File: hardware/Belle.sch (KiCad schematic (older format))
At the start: 18 parts, among them P1 Bell CONN, P2 Battery CONN, P3 Flashing CONN, U1 74AHC1G14, U2 ESP-12, U3 AP2112

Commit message: fix
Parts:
- C3, C4: footprint (none) -> Capacitors_SMD:C_1206_HandSoldering
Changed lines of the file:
@@
 $EndComp
 $Comp
-L GND #PWR8
+L GND #PWR01
 U 1 1 58BBCCFC
 P 5900 4700
-F 0 "#PWR8" H 5900 4450 50  0001 C CNN
+F 0 "#PWR01" H 5900 4450 50  0001 C CNN
 F 1 "GND" H 5900 4550 50  0000 C CNN
 F 2 "" H 5900 4700 50  0000 C CNN
@@
 $EndComp
 $Comp
-L +3.3V #PWR7
+L +3.3V #PWR02
 U 1 1 58BBCD12
 P 5900 2800
-F 0 "#PWR7" H 5900 2650 50  0001 C CNN
+F 0 "#PWR02" H 5900 2650 50  0001 C CNN
 F 1 "+3.3V" H 5900 2940 50  0000 C CNN
 F 2 "" H 5900 2800 50  0000 C CNN
@@
 $EndComp
 $Comp
-L GND #PWR9
+L GND #PWR03
 U 1 1 58BBCDC5
 P 6650 3000
-F 0 "#PWR9" H 6650 2750 50  0001 C CNN
+F 0 "#PWR03" H 6650 2750 50  0001 C CNN
 F 1 "GND" H 6650 2850 50  0000 C CNN
 F 2 "" H 6650 3000 50  0000 C CNN
@@
 $EndComp
 $Comp
-L GND #PWR5
+L GND #PWR04
 U 1 1 58BBD0DA
 P 3600 3800
-F 0 "#PWR5" H 3600 3550 50  0001 C CNN
+F 0 "#PWR04" H 3600 3550 50  0001 C CNN
 F 1 "GND" H 3600 3650 50  0000 C CNN
 F 2 "" H 3600 3800 50  0000 C CNN
@@
 $EndComp
 $Comp
-L +3.3V #PWR4
+L +3.3V #PWR05
 U 1 1 58BBD0F6
 P 3600 3150
-F 0 "#PWR4" H 3600 3000 50  0001 C CNN
+F 0 "#PWR05" H 3600 3000 50  0001 C CNN
 F 1 "+3.3V" H 3600 3290 50  0000 C CNN
 F 2 "" H 3600 3150 50  0000 C CNN
@@
 $EndComp
 $Comp
-L GND #PWR3
+L GND #PWR06
 U 1 1 58BBD1A3
 P 3100 4000
-F 0 "#PWR3" H 3100 3750 50  0001 C CNN
+F 0 "#PWR06" H 3100 3750 50  0001 C CNN
 F 1 "GND" H 3100 3850 50  0000 C CNN
 F 2 "" H 3100 4000 50  0000 C CNN
@@
 $EndComp
 $Comp
-L +3.3V #PWR1
+L +3.3V #PWR07
 U 1 1 58BBD349
 P 2400 2900
-F 0 "#PWR1" H 2400 2750 50  0001 C CNN
+F 0 "#PWR07" H 2400 2750 50  0001 C CNN
 F 1 "+3.3V" H 2400 3040 50  0000 C CNN
 F 2 "" H 2400 2900 50  0000 C CNN
@@
 $EndComp
 $Comp
-L GND #PWR2
+L GND #PWR08
 U 1 1 58BBD44E
 P 2400 3750
-F 0 "#PWR2" H 2400 3500 50  0001 C CNN
+F 0 "#PWR08" H 2400 3500 50  0001 C CNN
 F 1 "GND" H 2400 3600 50  0000 C CNN
 F 2 "" H 2400 3750 50  0000 C CNN
@@
 $EndComp
 $Comp
-L +3.3V #PWR6
+L +3.3V #PWR09
 U 1 1 58BBD4B2
 P 4350 3700
-F 0 "#PWR6" H 4350 3550 50  0001 C CNN
+F 0 "#PWR09" H 4350 3550 50  0001 C CNN
 F 1 "+3.3V" H 4350 3840 50  0000 C CNN
 F 2 "" H 4350 3700 50  0000 C CNN
@@
 $EndComp
 $Comp
-L +3.3V #PWR14
+L +3.3V #PWR010
 U 1 1 58BBD5B6
 P 7450 3900
-F 0 "#PWR14" H 7450 3750 50  0001 C CNN
+F 0 "#PWR010" H 7450 3750 50  0001 C CNN
 F 1 "+3.3V" H 7450 4040 50  0000 C CNN
 F 2 "" H 7450 3900 50  0000 C CNN
@@
 $EndComp
 $Comp
-L GND #PWR10
+L GND #PWR011
 U 1 1 58BBD6CB
 P 6800 4400
-F 0 "#PWR10" H 6800 4150 50  0001 C CNN
+F 0 "#PWR011" H 6800 4150 50  0001 C CNN
 F 1 "GND" H 6800 4250 50  0000 C CNN
 F 2 "" H 6800 4400 50  0000 C CNN
@@
 $EndComp
 $Comp
-L +3.3V #PWR13
+L +3.3V #PWR012
 U 1 1 58BBDA6C
 P 7150 4450
-F 0 "#PWR13" H 7150 4300 50  0001 C CNN
+F 0 "#PWR012" H 7150 4300 50  0001 C CNN
 F 1 "+3.3V" H 7150 4590 50  0000 C CNN
 F 2 "" H 7150 4450 50  0000 C CNN
@@
 $EndComp
 $Comp
-L GND #PWR15
+L GND #PWR013
 U 1 1 58BBDB81
 P 7600 5250
-F 0 "#PWR15" H 7600 5000 50  0001 C CNN
+F 0 "#PWR013" H 7600 5000 50  0001 C CNN
 F 1 "GND" H 7600 5100 50  0000 C CNN
 F 2 "" H 7600 5250 50  0000 C CNN
@@
 $EndComp
 $Comp
-L GND #PWR17
+L GND #PWR014
 U 1 1 58BBDD34
 P 8400 5150
-F 0 "#PWR17" H 8400 4900 50  0001 C CNN
+F 0 "#PWR014" H 8400 4900 50  0001 C CNN
 F 1 "GND" H 8400 5000 50  0000 C CNN
 F 2 "" H 8400 5150 50  0000 C CNN
@@
 $EndComp
 $Comp
-L GND #PWR16
+L GND #PWR015
 U 1 1 58BBDF88
 P 8200 4000
-F 0 "#PWR16" H 8200 3750 50  0001 C CNN
+F 0 "#PWR015" H 8200 3750 50  0001 C CNN
 F 1 "GND" H 8200 3850 50  0000 C CNN
 F 2 "" H 8200 4000 50  0000 C CNN
@@
 $EndComp
 $Comp
-L +3.3V #PWR12
+L +3.3V #PWR016
 U 1 1 58BBED05
 P 7150 2700
-F 0 "#PWR12" H 7150 2550 50  0001 C CNN
+F 0 "#PWR016" H 7150 2550 50  0001 C CNN
 F 1 "+3.3V" H 7150 2840 50  0000 C CNN
 F 2 "" H 7150 2700 50  0000 C CNN
@@
 NoConn ~ 6800 3800
 $Comp
-L PWR_FLAG #FLG1
+L PWR_FLAG #FLG017
 U 1 1 58BBEBAB
 P 8200 4850
-F 0 "#FLG1" H 8200 4945 50  0001 C CNN
+F 0 "#FLG017" H 8200 4945 50  0001 C CNN
 F 1 "PWR_FLAG" H 8200 5030 50  0000 C CNN
 F 2 "" H 8200 4850 50  0000 C CNN
@@
 F 0 "C4" H 8310 4370 50  0000 L CNN
 F 1 "1u" H 8310 4220 50  0000 L CNN
-F 2 "" H 8300 4300 50  0000 C CNN
+F 2 "Capacitors_SMD:C_1206_HandSoldering" H 8300 4300 50  0001 C CNN
 F 3 "" H 8300 4300 50  0000 C CNN
 	1    8300 4300
@@
 Connection ~ 8050 4300
 $Comp
-L GND #PWR18
+L GND #PWR018
 U 1 1 58CE4ED3
 P 8500 4300
-F 0 "#PWR18" H 8500 4050 50  0001 C CNN
+F 0 "#PWR018" H 8500 4050 50  0001 C CNN
 F 1 "GND" H 8500 4150 50  0000 C CNN
 F 2 "" H 8500 4300 50  0000 C CNN
@@
 F 0 "C3" H 6810 4870 50  0000 L CNN
 F 1 "1u" H 6810 4720 50  0000 L CNN
-F 2 "" H 6800 4800 50  0000 C CNN
+F 2 "Capacitors_SMD:C_1206_HandSoldering" H 6800 4800 50  0001 C CNN
 F 3 "" H 6800 4800 50  0000 C CNN
 	1    6800 4800
@@
 $EndComp
 $Comp
-L GND #PWR11
+L GND #PWR019
 U 1 1 58CE504A
 P 6800 5000
-F 0 "#PWR11" H 6800 4750 50  0001 C CNN
+F 0 "#PWR019" H 6800 4750 50  0001 C CNN
 F 1 "GND" H 6800 4850 50  0000 C CNN
 F 2 "" H 6800 5000 50  0000 C CNN

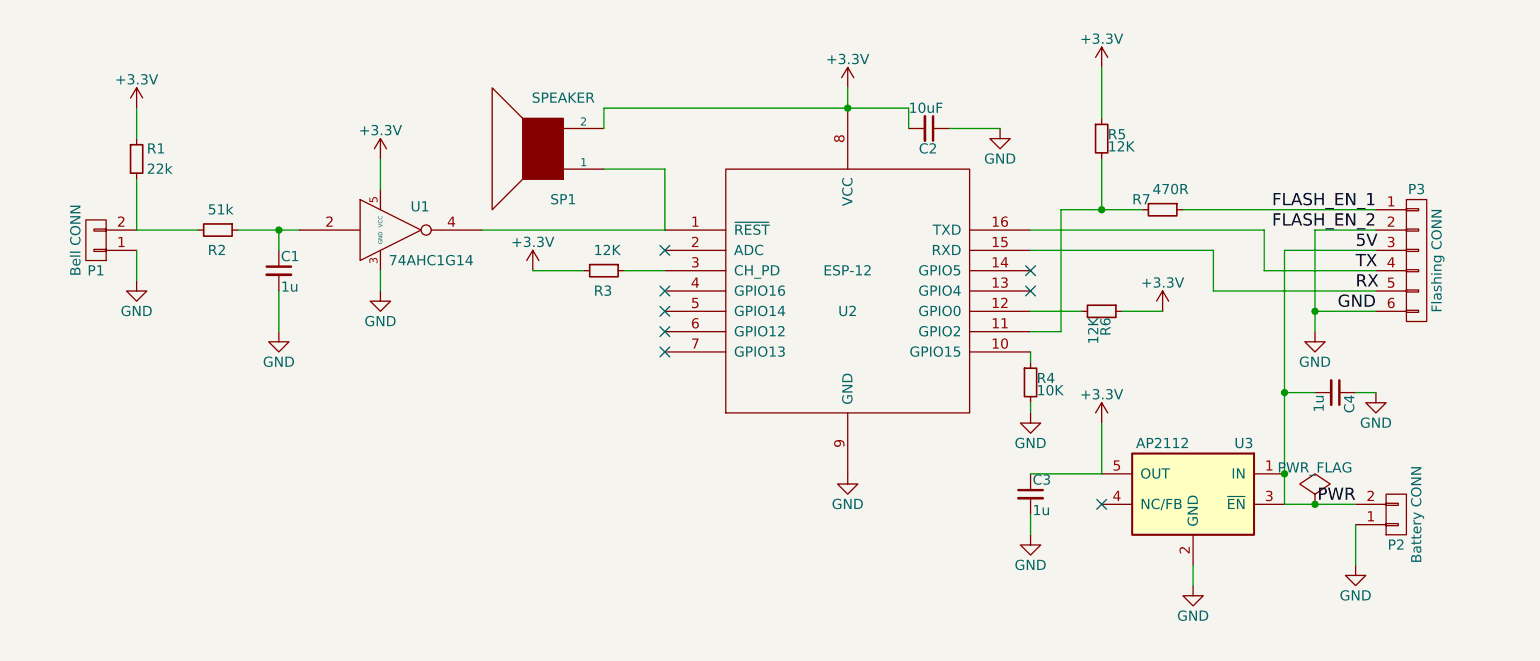
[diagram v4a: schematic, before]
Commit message: add notes to the schematic. close #4
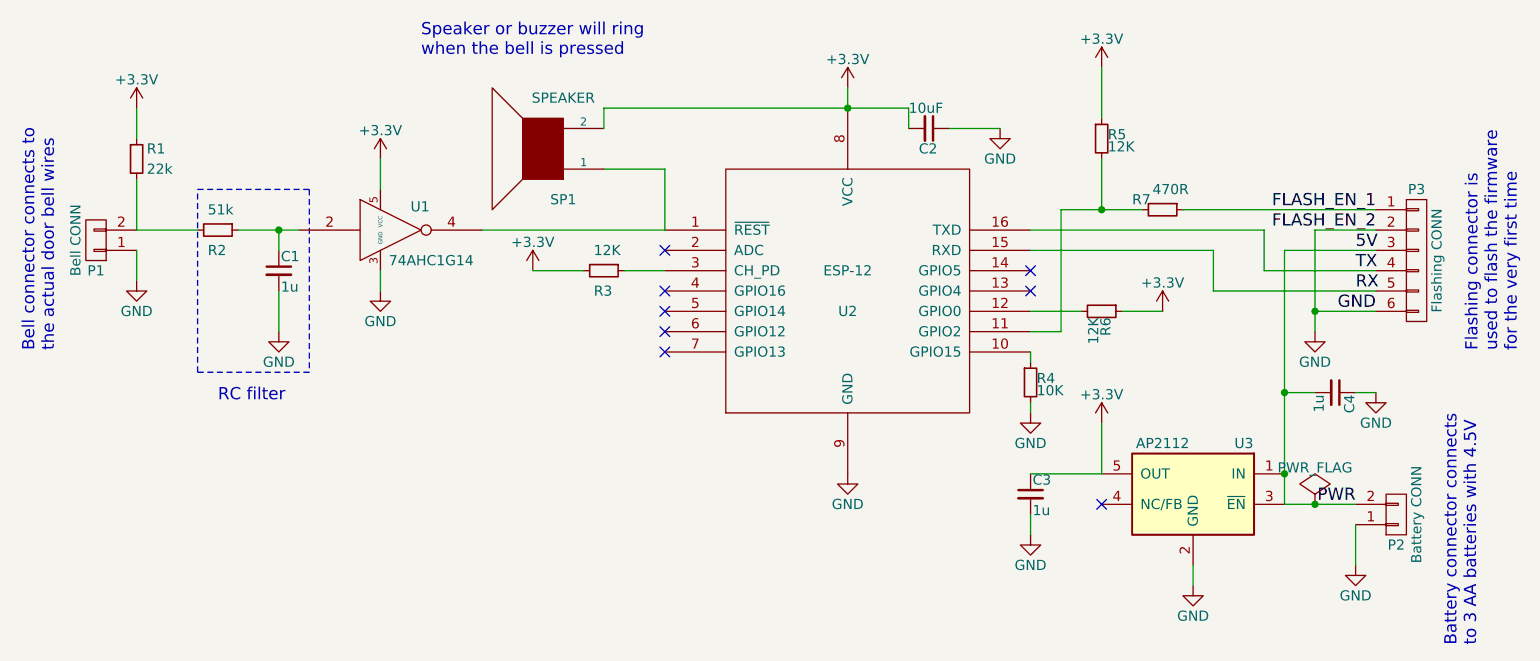
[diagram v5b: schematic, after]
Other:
- note added: "Battery connector connects \nto 3 AA batteries with 4.5V"
- note added: "Bell connector connects to \nthe actual door bell wires"
- note added: "Flashing connector is\nused to flash the firmware\nfor the very first time"
- note added: "RC filter"
- note added: "Speaker or buzzer will ring \nwhen the bell is pressed"
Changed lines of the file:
@@
 Wire Wire Line
 	6800 4900 6800 5000
+Text Notes 3800 2650 0    60   ~ 0
+Speaker or buzzer will ring \nwhen the bell is pressed
+Text Notes 9200 4100 1    60   ~ 0
+Flashing connector is\nused to flash the firmware\nfor the very first time
+Text Notes 2000 4100 1    60   ~ 0
+Bell connector connects to \nthe actual door bell wires
+Text Notes 9000 5550 1    60   ~ 0
+Battery connector connects \nto 3 AA batteries with 4.5V
+Wire Notes Line
+	2700 3300 3250 3300
+Wire Notes Line
+	3250 3300 3250 4200
+Wire Notes Line
+	3250 4200 2700 4200
+Wire Notes Line
+	2700 4200 2700 3300
+Text Notes 2800 4350 0    60   ~ 0
+RC filter
 $EndSCHEMATC

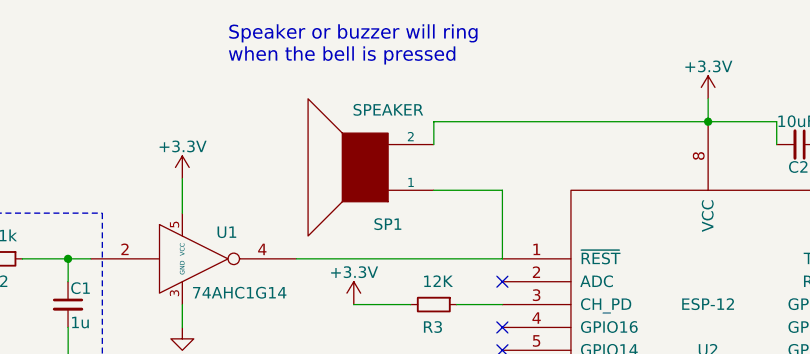
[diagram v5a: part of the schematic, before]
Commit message: rename speaker to buzzer. close #9
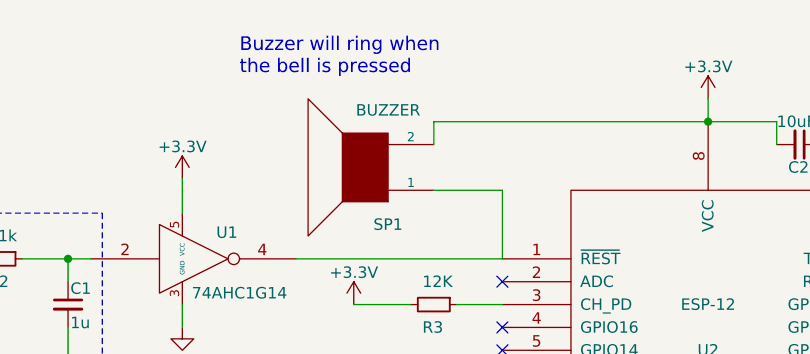
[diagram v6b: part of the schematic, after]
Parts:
- SP1: value SPEAKER -> BUZZER
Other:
- note added: "Buzzer will ring when \nthe bell is pressed"
- note removed: "Speaker or buzzer will ring \nwhen the bell is pressed"
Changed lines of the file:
@@
 P 4400 3100
 F 0 "SP1" H 4300 3350 50  0000 C CNN
-F 1 "SPEAKER" H 4300 2850 50  0000 C CNN
+F 1 "BUZZER" H 4300 2850 50  0000 C CNN
 F 2 "Belle:prosignal_buzzer" H 4400 3100 50  0001 C CNN
 F 3 "" H 4400 3100 50  0000 C CNN
@@
 Wire Wire Line
 	6800 4900 6800 5000
-Text Notes 3800 2650 0    60   ~ 0
-Speaker or buzzer will ring \nwhen the bell is pressed
+Text Notes 3850 2700 0    60   ~ 0
+Buzzer will ring when \nthe bell is pressed
 Text Notes 9200 4100 1    60   ~ 0
 Flashing connector is\nused to flash the firmware\nfor the very first time
